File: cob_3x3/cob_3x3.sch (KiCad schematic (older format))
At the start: 14 parts, among them J1 Conn_01x03, J2 Conn_01x03, J3 Anderson_two_redblack, J4 Anderson_two_redblack, U1 5V_REG_AP7370-50W5-7

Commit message: Add TVCs and power indicator to schematic.
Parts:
- added D10, D9: D_TVS, symbol Device:D_Schottky
- added D11: LED, symbol Device:LED
- added R4: R, symbol Device:R
- added TH1: Thermistor_PTC, symbol Device:Thermistor_PTC
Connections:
- net +12V: now also D9.1 (K), TH1.1; no longer C2.1, J3.1, J4.1
- net +5V: now also D11.2 (A)
- net GND: now also D10.2 (A), D9.2 (A), R4.2
- net SIGNAL_IN: now also D10.1 (K)
- new net: D11.1 (K), R4.1
- new net 12V_RAW: C2.1, J3.1, J4.1, TH1.2
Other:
- moved on the sheet: C1, C2, J3, J4

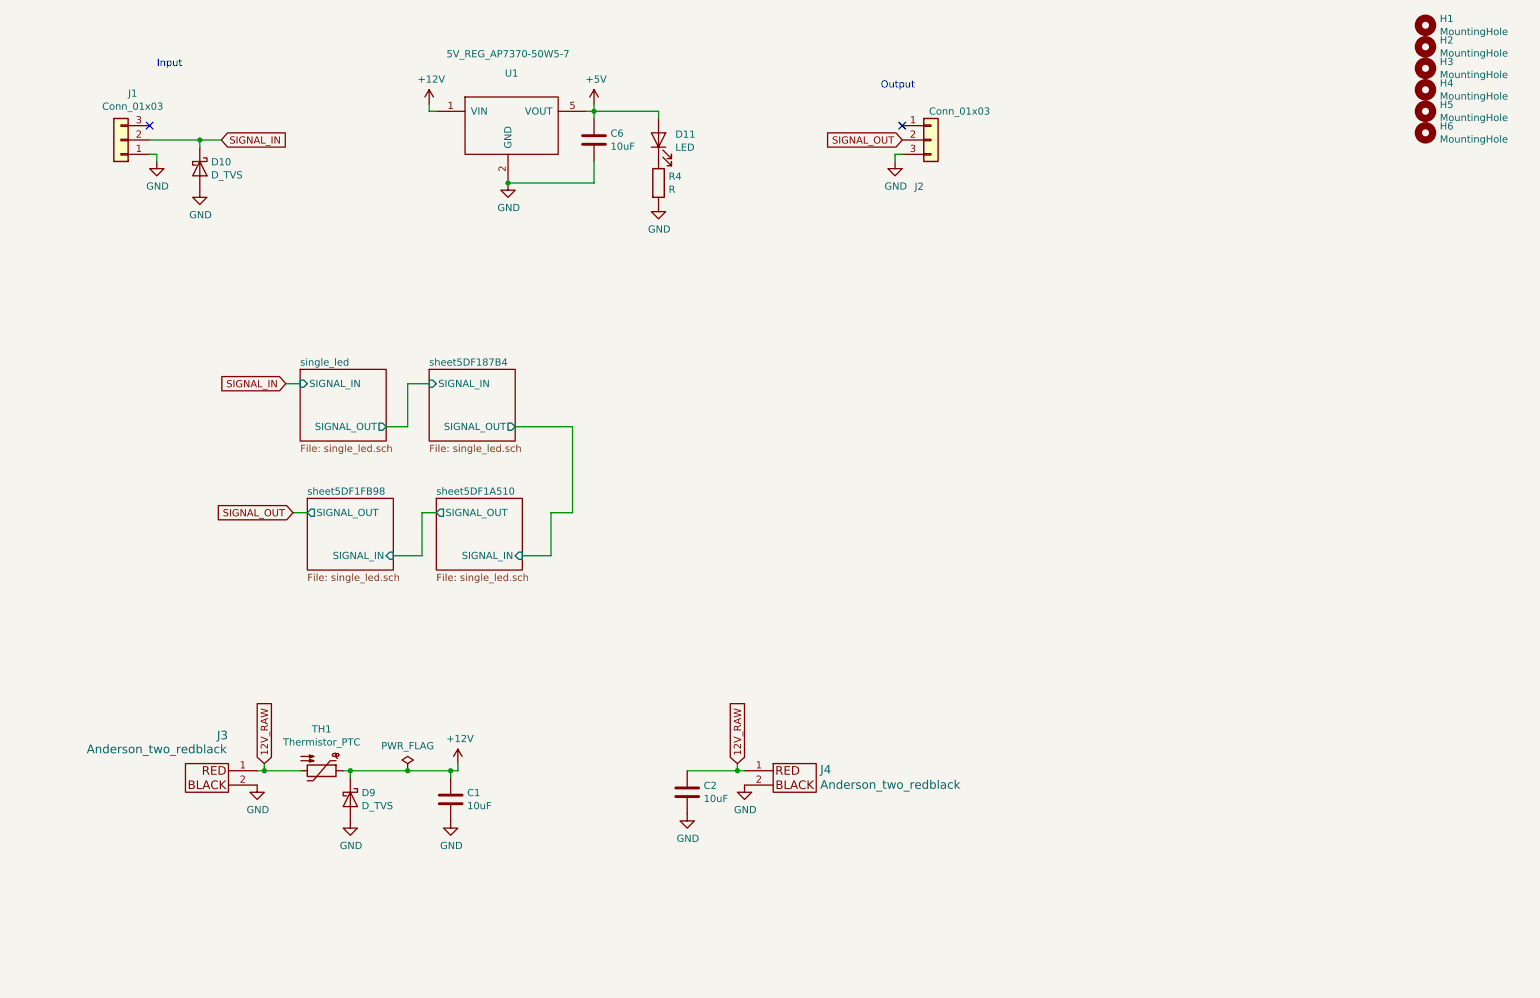
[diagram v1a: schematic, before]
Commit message: Schematic and footprints ready for v1.0:
- Added board-to-board connectors for chaining a 2x2 array of 2x2
boards.
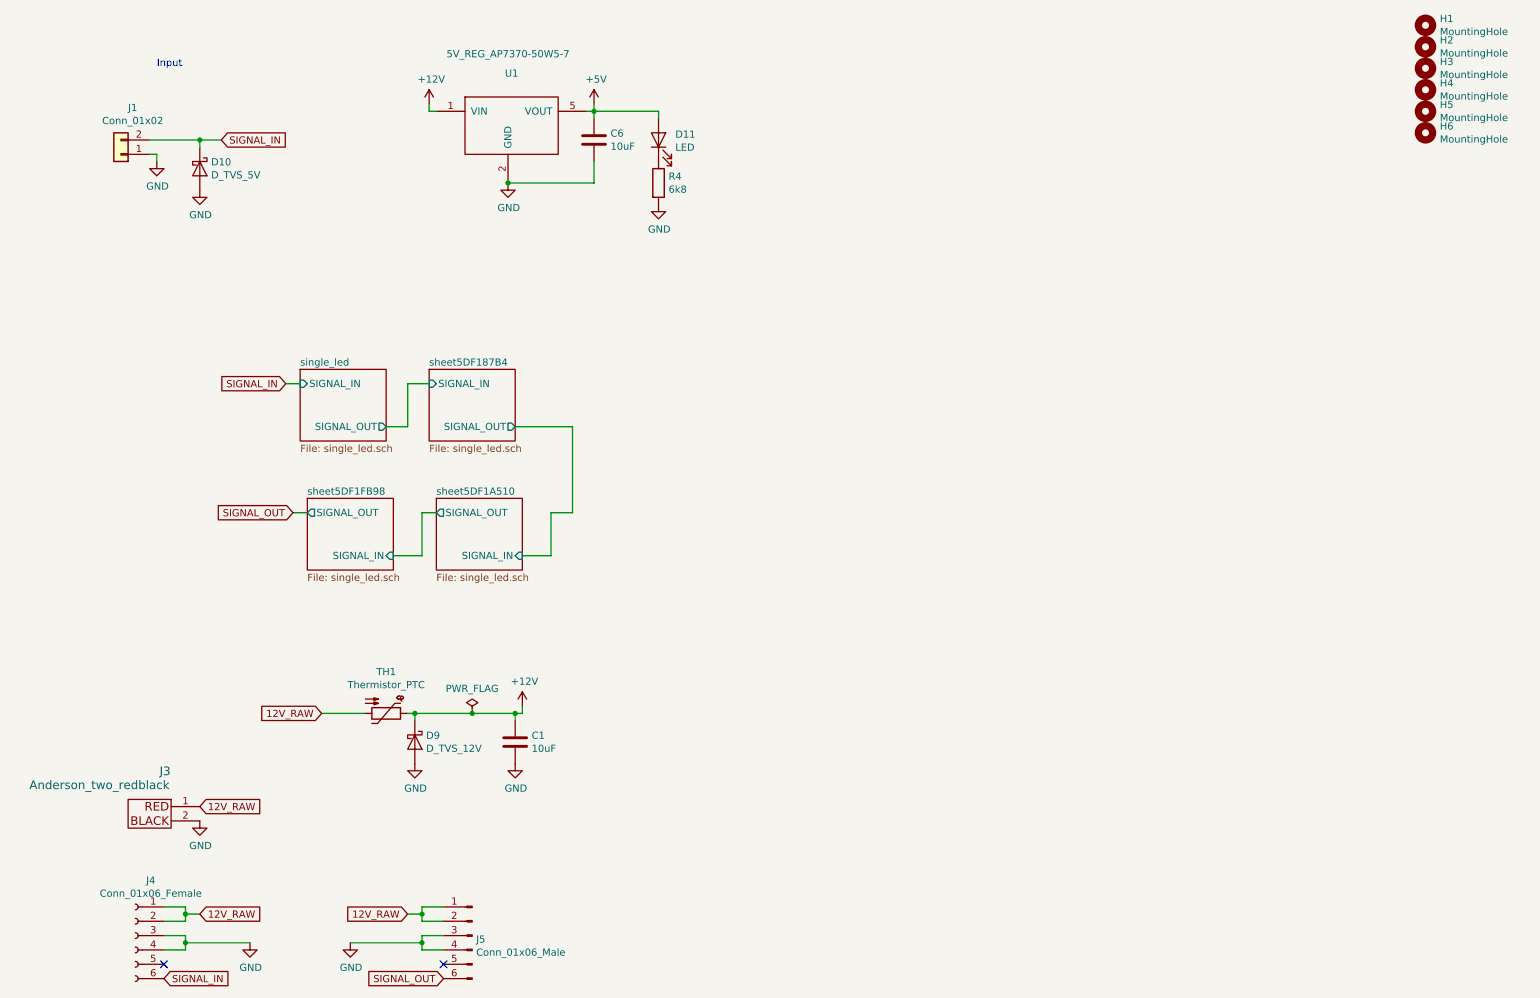
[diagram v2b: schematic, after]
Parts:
- removed C2: 10uF, symbol Device:C
- removed J1, J2: Conn_01x03, Connector_PinHeader_2.54mm:PinHeader_1x03_P2.54mm_Vertical, symbol Connector_Generic:Conn_01x03
- removed J4: Anderson_two_redblack, symbol Homebrew:Anderson_two_redblack_sink
- added J1: Conn_01x02, Connector_PinHeader_2.54mm:PinHeader_1x02_P2.54mm_Vertical, symbol Connector_Generic:Conn_01x02
- added J4: Conn_01x06_Female, Connector_PinSocket_2.54mm:PinSocket_1x06_P2.54mm_Horizontal, symbol Connector:Conn_01x06_Female
- added J5: Conn_01x06_Male, Connector_PinHeader_2.54mm:PinHeader_1x06_P2.54mm_Horizontal, symbol Connector:Conn_01x06_Male
- C1: footprint (none) -> Capacitor_SMD:C_0805_2012Metric
- D10: value D_TVS -> D_TVS_5V; footprint (none) -> homebrew:SOD-923
- D11: footprint (none) -> LED_SMD:LED_0603_1608Metric_Pad1.05x0.95mm_HandSolder
- D9: value D_TVS -> D_TVS_12V; footprint (none) -> Diode_SMD:D_SOD-323_HandSoldering
- J3: footprint (none) -> homebrew:Anderson_1337G3_right_angle_bottom_two
- R4: value R -> 6k8; footprint (none) -> Resistor_SMD:R_0603_1608Metric
- TH1: footprint (none) -> Resistor_SMD:R_1812_4532Metric
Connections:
- net 12V_RAW: now also J4.1 (Pin_1), J4.2 (Pin_2), J5.1 (Pin_1), J5.2 (Pin_2)
- net GND: now also J1.1 (Pin_1), J4.3 (Pin_3), J4.4 (Pin_4), J5.3 (Pin_3), J5.4 (Pin_4)
- net SIGNAL_IN: now also J1.2 (Pin_2), J4.6 (Pin_6)
- net SIGNAL_OUT: now also J5.6 (Pin_6)
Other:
- note removed: "Output"
- moved on the sheet: C1, D9, J3, TH1
